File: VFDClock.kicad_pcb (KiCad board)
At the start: 2 copper layers, 76.2 x 53.3 mm, 21 parts, among them J1 Barrel_Jack_MountingPin, P1 Power, P2 Analog, P3 Digital, P4 Digital, Q1 VFD_LD8035E, Q2 VFD_LD8035E, Q3 VFD_LD8035E, Q4 VFD_LD8035E, Q5 VFD_LD8035E, Q6 VFD_LD8035E, U1 IC_HT16K33

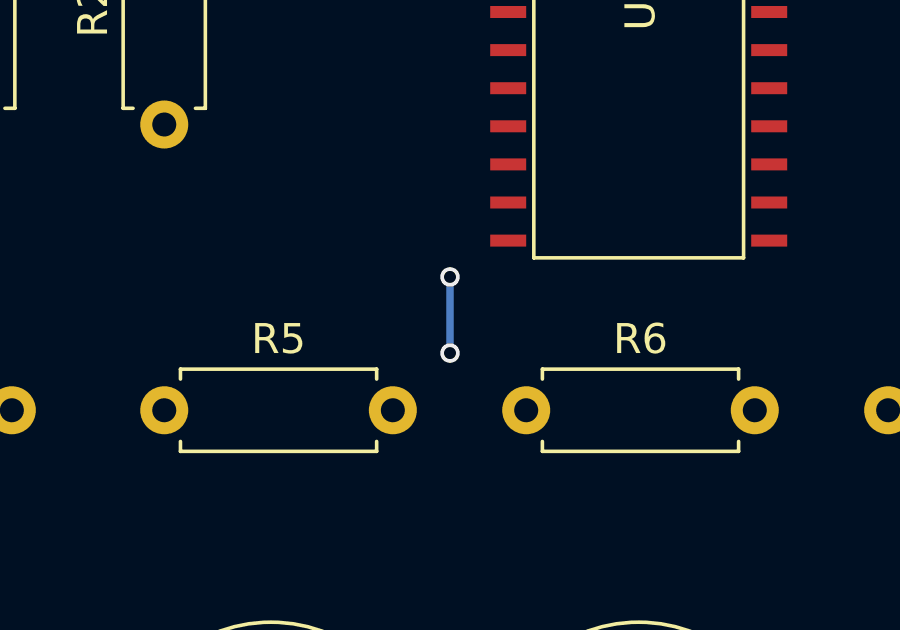
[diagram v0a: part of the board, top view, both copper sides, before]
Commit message: 余分なビアを削除
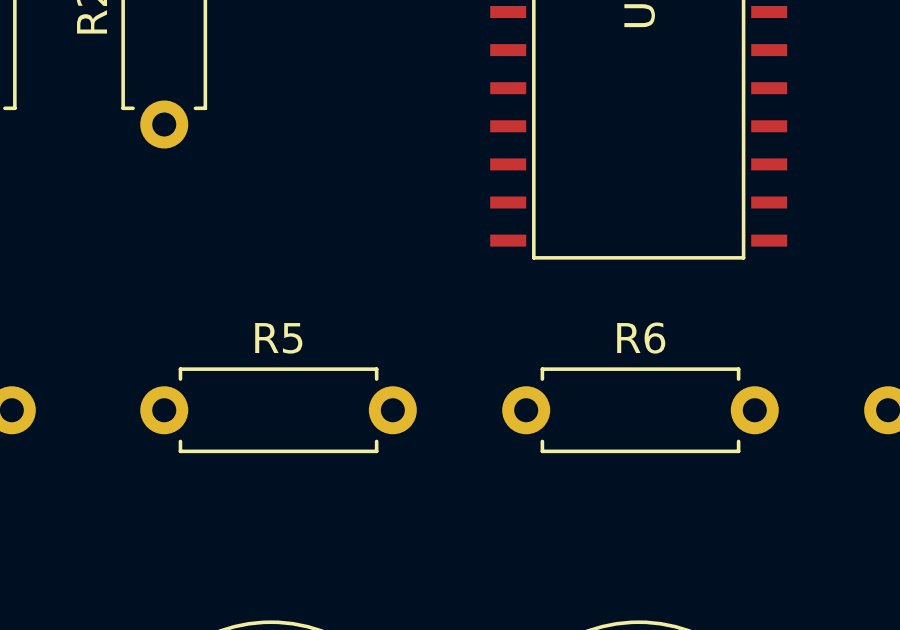
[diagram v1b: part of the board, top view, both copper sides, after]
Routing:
- net GND: track 2.54 -> 0.00 mm, vias 2 -> 0
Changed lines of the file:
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@@
     (thickness 1.6)
     (drawings 11)
-    (tracks 3)
+    (tracks 0)
     (zones 0)
     (modules 21)
@@
   (gr_line (start 175.514 73.025) (end 110.998 73.025) (angle 90) (layer Edge.Cuts) (width 0.15))
   (gr_line (start 104.648 82.55) (end 120.523 82.55) (angle 90) (layer Dwgs.User) (width 0.15))
-  (via (at 149.098 98.425) (size 0.65) (drill 0.4) (layers F.Cu B.Cu) (net 2))
-  (via (at 149.098 100.965) (size 0.65) (drill 0.4) (layers F.Cu B.Cu) (net 2))
-  (segment (start 149.098 98.425) (end 149.098 100.965) (width 0.25) (layer B.Cu) (net 2))
 )

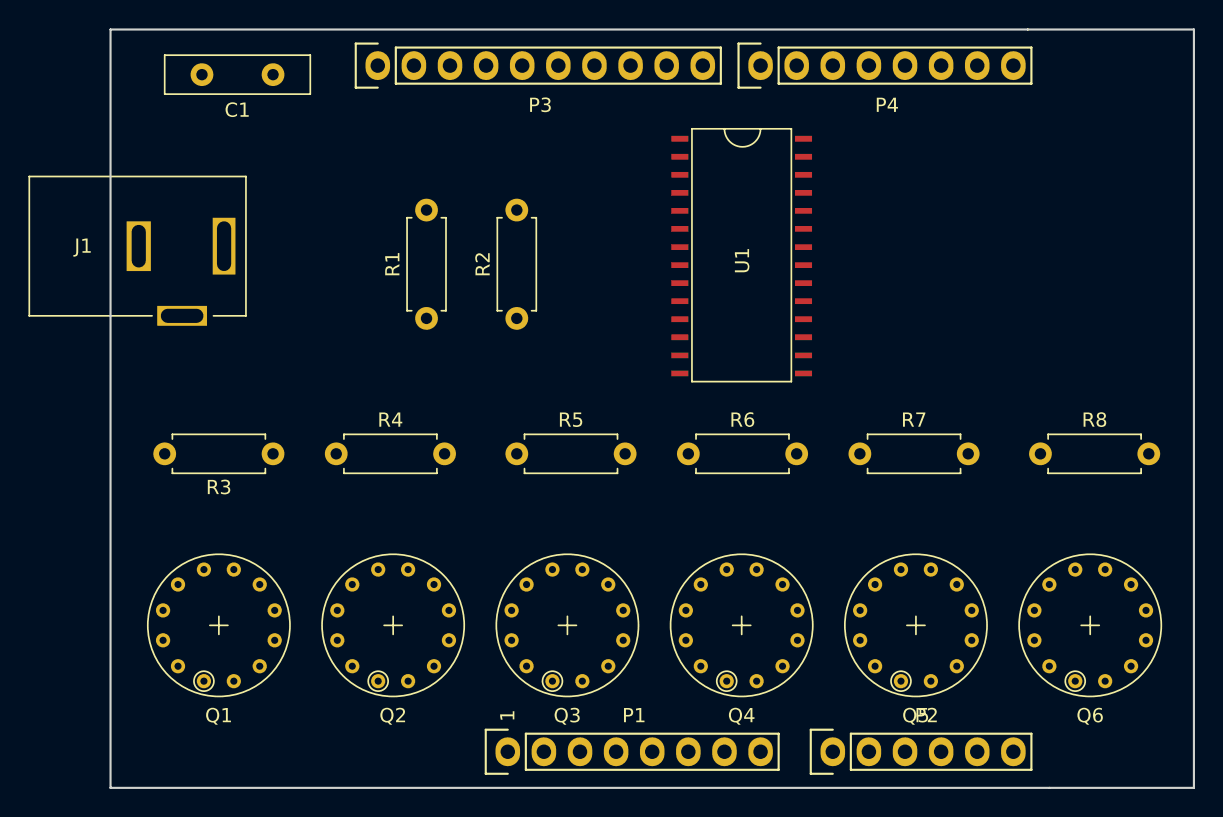
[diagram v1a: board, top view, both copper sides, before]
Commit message: RTCを追加
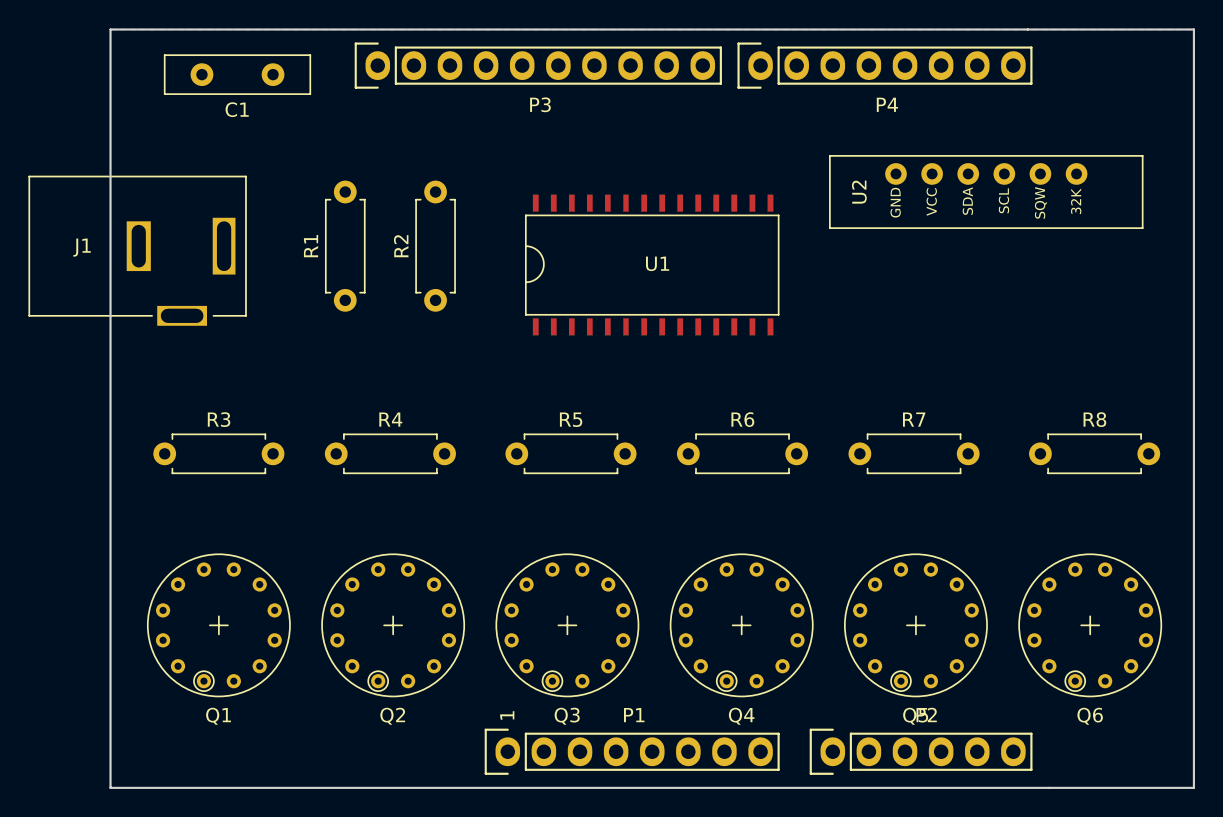
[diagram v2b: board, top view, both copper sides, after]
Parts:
- added U2: RTC_DS3231, #MyFootPrints:RTC_DS3231_Vertical, F.Cu at (172.6, 87.0)
- moved U1 17.6 mm to (140.2, 93.3), turned to 90 degrees
- moved R3 7.62 mm to (114.8, 102.9), turned to 0 degrees
- moved R1 5.85 mm to (127.5, 92.1)
- moved R2 5.85 mm to (133.9, 92.1)
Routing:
- added copper zone on B.Cu, net GND
- added copper zone on F.Cu, net GND
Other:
- net class GND added: clearance 0.2, trace_width 0.6, via_dia 0.65, via_drill 0.4

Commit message: 自動配線
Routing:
- net /a: track 0.00 -> 121.7 mm
- net /dp: track 0.00 -> 120.7 mm
- net /e: track 0.00 -> 118.6 mm
- net /d: track 0.00 -> 115.2 mm, vias 0 -> 1
- net +5V: track 0.00 -> 105.8 mm
- net /c: track 0.00 -> 104.7 mm, vias 0 -> 1
- net +12V: track 0.00 -> 102.9 mm
- net /g: track 0.00 -> 102.6 mm, vias 0 -> 1
- net /b: track 0.00 -> 102.1 mm, vias 0 -> 1
- net /f: track 0.00 -> 96.1 mm, vias 0 -> 1
- net Net-(Q5-Pad3): track 0.00 -> 69.1 mm
- net /A5(SCL): track 0.00 -> 61.6 mm
- net Net-(Q6-Pad3): track 0.00 -> 50.7 mm
- net /A4(SDA): track 0.00 -> 49.7 mm
- net Net-(Q1-Pad3): track 0.00 -> 35.3 mm, vias 0 -> 1
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
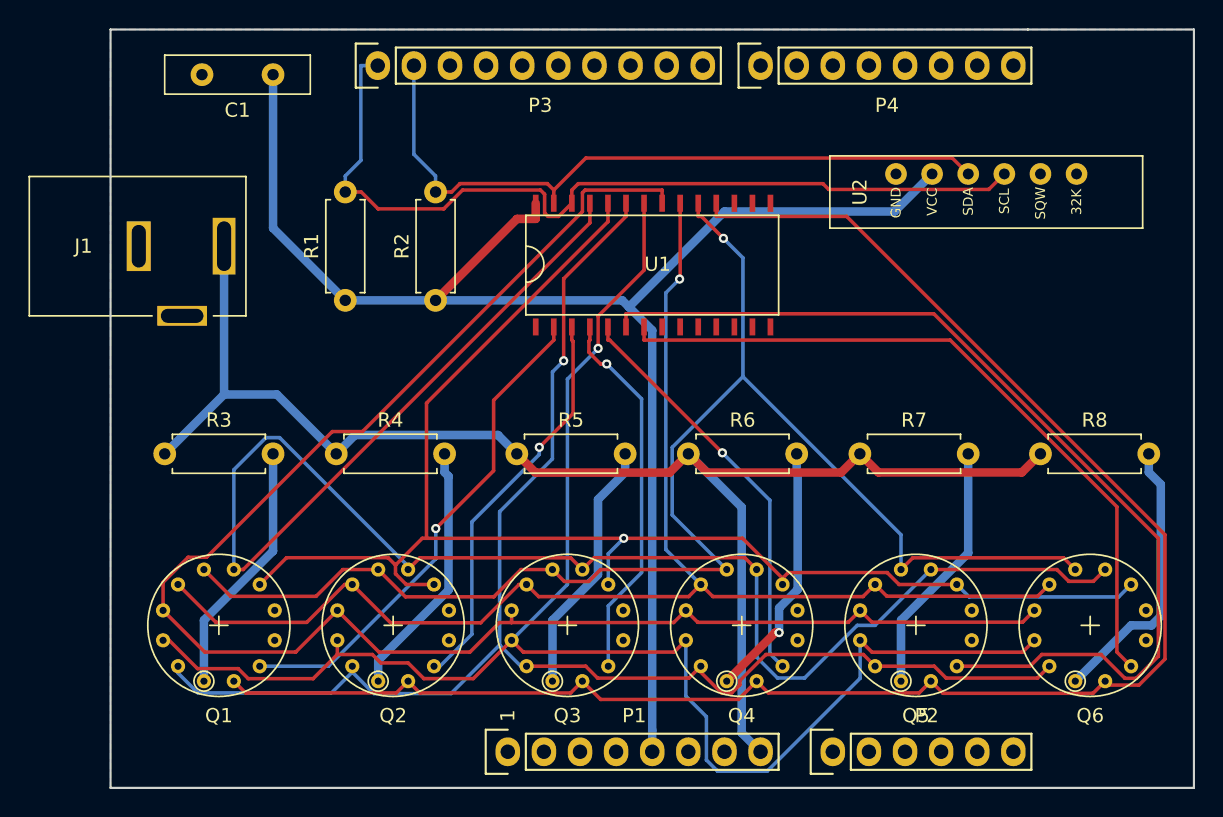
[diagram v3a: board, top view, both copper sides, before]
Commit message: 配線を修正
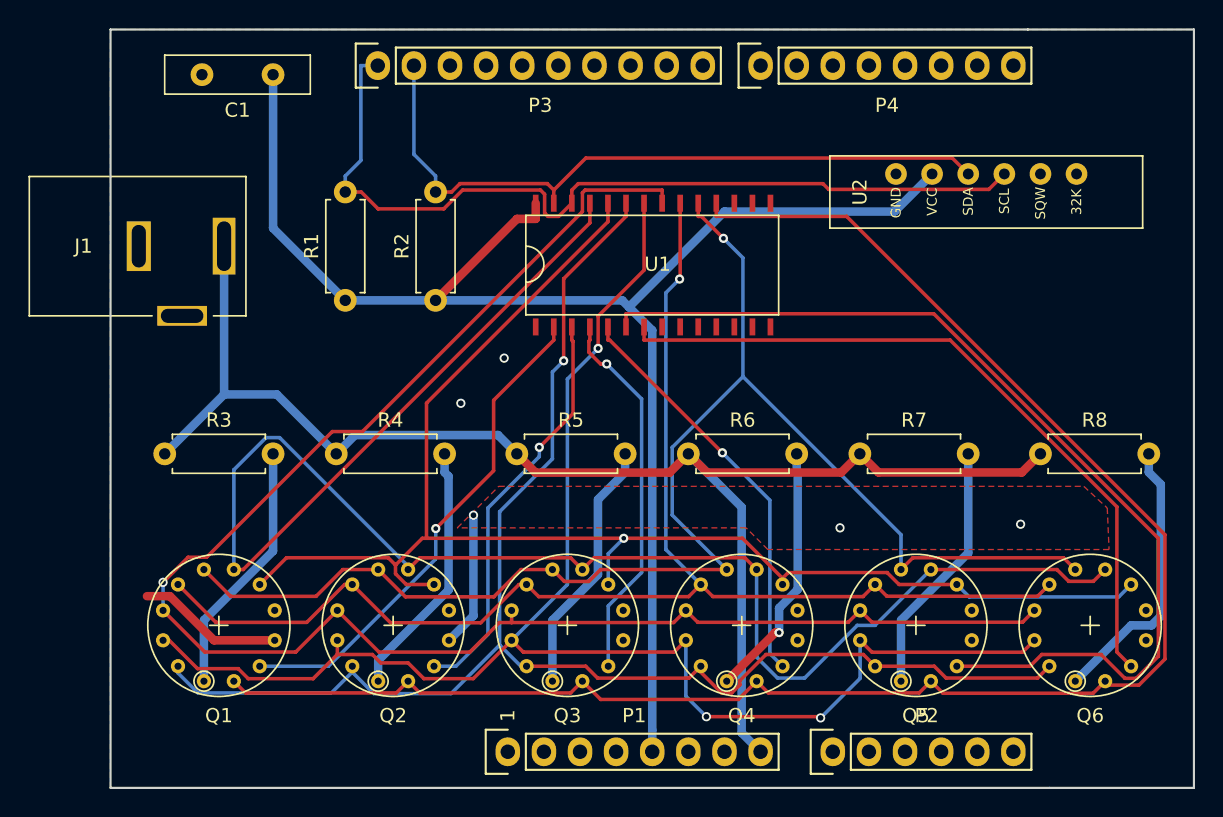
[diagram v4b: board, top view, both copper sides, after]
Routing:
- net GND: track 0.00 -> 19.8 mm, vias 0 -> 5
- net /d: track 115.2 -> 110.3 mm, vias 1 -> 3
- net Net-(Q2-Pad3): track 28.2 -> 29.3 mm
- net /e: vias 0 -> 1

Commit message: GND修正
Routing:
- net GND: track 19.8 -> 47.5 mm, vias 5 -> 4
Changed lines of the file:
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@@
     (thickness 1.6)
     (drawings 11)
-    (tracks 375)
+    (tracks 382)
     (zones 0)
     (modules 22)
@@
   (segment (start 122.428 86.995) (end 127.508 92.075) (width 0.6) (layer B.Cu) (net 1))
   (segment (start 140.903 85.245) (end 140.903 86.3453) (width 0.6) (layer F.Cu) (net 1))
-  (via (at 138.684 96.139) (size 0.65) (drill 0.4) (layers F.Cu B.Cu) (net 2))
-  (via (at 135.636 99.314) (size 0.65) (drill 0.4) (layers F.Cu B.Cu) (net 2))
-  (via (at 162.306 108.077) (size 0.65) (drill 0.4) (layers F.Cu B.Cu) (net 2))
-  (via (at 175.006 107.823) (size 0.65) (drill 0.4) (layers F.Cu B.Cu) (net 2))
   (segment (start 115.172478 112.883158) (end 113.557842 112.883158) (width 0.6) (layer F.Cu) (net 2))
   (segment (start 122.543523 115.986841) (end 118.276161 115.986841) (width 0.6) (layer F.Cu) (net 2))
   (segment (start 118.276161 115.986841) (end 115.172478 112.883158) (width 0.6) (layer F.Cu) (net 2))
-  (segment (start 134.800523 115.986841) (end 136.525 114.262364) (width 0.6) (layer B.Cu) (net 2))
-  (segment (start 136.525 114.262364) (end 136.525 107.188) (width 0.6) (layer B.Cu) (net 2))
-  (segment (start 136.525 107.188) (end 136.525 107.188) (width 0.6) (layer B.Cu) (net 2))
-  (via (at 136.525 107.188) (size 0.65) (drill 0.4) (layers F.Cu B.Cu) (net 2))
+  (segment (start 136.525 102.743) (end 136.525 102.743) (width 0.6) (layer B.Cu) (net 2))
+  (via (at 136.525 102.743) (size 0.65) (drill 0.4) (layers F.Cu B.Cu) (net 2))
+  (segment (start 136.525 98.323) (end 140.903 93.945) (width 0.6) (layer F.Cu) (net 2))
+  (segment (start 136.525 102.743) (end 136.525 98.323) (width 0.6) (layer F.Cu) (net 2))
+  (segment (start 136.525 114.262364) (end 134.800523 115.986841) (width 0.6) (layer B.Cu) (net 2))
+  (segment (start 136.525 102.743) (end 136.525 114.262364) (width 0.6) (layer B.Cu) (net 2))
+  (segment (start 136.525 98.323) (end 136.525 98.323) (width 0.6) (layer F.Cu) (net 2))
+  (via (at 136.525 98.323) (size 0.65) (drill 0.4) (layers F.Cu B.Cu) (net 2))
+  (segment (start 159.314523 115.986841) (end 161.925 113.376364) (width 0.6) (layer B.Cu) (net 2))
+  (segment (start 161.925 113.376364) (end 161.925 109.474) (width 0.6) (layer B.Cu) (net 2))
+  (segment (start 161.925 109.474) (end 161.925 109.474) (width 0.6) (layer B.Cu) (net 2))
+  (via (at 161.925 109.474) (size 0.65) (drill 0.4) (layers F.Cu B.Cu) (net 2))
+  (segment (start 161.925 109.474) (end 165.481 105.918) (width 0.6) (layer F.Cu) (net 2))
+  (segment (start 165.481 105.918) (end 165.481 105.918) (width 0.6) (layer F.Cu) (net 2))
+  (via (at 165.481 105.918) (size 0.65) (drill 0.4) (layers F.Cu B.Cu) (net 2))
   (segment (start 133.858 84.455) (end 133.858 83.3297) (width 0.25) (layer B.Cu) (net 3))
   (segment (start 132.334 75.565) (end 132.334 81.8057) (width 0.25) (layer B.Cu) (net 3))
@@
   (segment (start 184.8673 114.2873) (end 184.8673 105.0146) (width 0.6) (layer B.Cu) (net 25))
   (segment (start 184.8673 105.0146) (end 184.023 104.1703) (width 0.6) (layer B.Cu) (net 25))
-  (zone (net 2) (net_name GND) (layer B.Cu) (hatch edge 0.508)
-    (connect_pads (clearance 0.508))
-    (min_thickness 0.254)
-    (fill yes (arc_segments 32) (thermal_gap 0.508) (thermal_bridge_width 0.508))
-    (polygon
-      (pts
-        (xy 187.198 126.365) (xy 110.998 126.365) (xy 110.998 73.025) (xy 187.198 73.025)
-      )
-    )
-  )
   (zone (net 2) (net_name GND) (layer F.Cu) (hatch edge 0.508)
     (connect_pads (clearance 0.508))
@@
       (pts
         (xy 187.198 126.365) (xy 110.998 126.365) (xy 110.998 73.025) (xy 187.198 73.025)
-      )
-    )
-  )
-  (zone (net 0) (net_name "") (layer F.Cu) (hatch edge 0.508)
-    (connect_pads (clearance 0.508))
-    (min_thickness 0.254)
-    (keepout (tracks allowed) (vias allowed) (copperpour not_allowed))
-    (fill (arc_segments 32) (thermal_gap 0.508) (thermal_bridge_width 0.508))
-    (polygon
-      (pts
-        (xy 142.113 92.71) (xy 140.843 92.71) (xy 142.113 91.44)
-      )
-    )
-  )
-  (zone (net 0) (net_name "") (layer F.Cu) (hatch edge 0.508)
-    (connect_pads (clearance 0.508))
-    (min_thickness 0.254)
-    (keepout (tracks allowed) (vias allowed) (copperpour not_allowed))
-    (fill (arc_segments 32) (thermal_gap 0.508) (thermal_bridge_width 0.508))
-    (polygon
-      (pts
-        (xy 142.494 93.218) (xy 140.462 93.218) (xy 140.462 92.837) (xy 142.113 91.186) (xy 142.367 91.186)
-      )
-    )
-  )
-  (zone (net 2) (net_name GND) (layer F.Cu) (hatch edge 0.508)
-    (connect_pads (clearance 0.508))
-    (min_thickness 0.254)
-    (fill yes (arc_segments 32) (thermal_gap 0.508) (thermal_bridge_width 0.508))
-    (polygon
-      (pts
-        (xy 181.102 106.68) (xy 181.229 109.601) (xy 157.226 109.601) (xy 155.702 108.077) (xy 135.382 108.077)
-        (xy 138.303 105.156) (xy 179.451 105.156)
       )
     )
@@
       )
     )
+  )
+  (zone (net 2) (net_name GND) (layer B.Cu) (hatch edge 0.508)
+    (connect_pads (clearance 0.508))
+    (min_thickness 0.254)
+    (fill yes (arc_segments 32) (thermal_gap 0.508) (thermal_bridge_width 0.508))
+    (polygon
+      (pts
+        (xy 187.198 126.365) (xy 110.998 126.365) (xy 110.998 73.025) (xy 187.198 73.025)
+      )
+    )
+  )
+  (zone (net 0) (net_name "") (layer B.Cu) (hatch edge 0.508)
+    (connect_pads (clearance 0.508))
+    (min_thickness 0.254)
+    (keepout (tracks allowed) (vias allowed) (copperpour not_allowed))
+    (fill (arc_segments 32) (thermal_gap 0.508) (thermal_bridge_width 0.508))
+    (polygon
+      (pts
+        (xy 138.43 103.124) (xy 139.446 104.14) (xy 137.16 106.68) (xy 137.033 115.316) (xy 135.89 116.586)
+        (xy 134.874 114.808) (xy 135.382 104.013) (xy 135.636 102.235) (xy 138.049 102.108)
+      )
+    )
+  )
+  (zone (net 0) (net_name "") (layer B.Cu) (hatch edge 0.508)
+    (connect_pads (clearance 0.508))
+    (min_thickness 0.254)
+    (keepout (tracks allowed) (vias allowed) (copperpour not_allowed))
+    (fill (arc_segments 32) (thermal_gap 0.508) (thermal_bridge_width 0.508))
+    (polygon
+      (pts
+        (xy 165.608 108.458) (xy 159.893 117.729) (xy 157.861 116.84) (xy 159.766 112.649) (xy 159.766 103.886)
+        (xy 160.274 103.251)
+      )
+    )
+  )
+  (zone (net 0) (net_name "") (layer F.Cu) (hatch edge 0.508)
+    (connect_pads (clearance 0.508))
+    (min_thickness 0.254)
+    (keepout (tracks allowed) (vias allowed) (copperpour not_allowed))
+    (fill (arc_segments 32) (thermal_gap 0.508) (thermal_bridge_width 0.508))
+    (polygon
+      (pts
+        (xy 141.224 95.25) (xy 137.668 98.679) (xy 137.541 103.886) (xy 133.731 107.442) (xy 133.731 99.568)
+        (xy 141.224 92.202)
+      )
+    )
+  )
+  (zone (net 0) (net_name "") (layer F.Cu) (hatch edge 0.508)
+    (connect_pads (clearance 0.508))
+    (min_thickness 0.254)
+    (keepout (tracks allowed) (vias allowed) (copperpour not_allowed))
+    (fill (arc_segments 32) (thermal_gap 0.508) (thermal_bridge_width 0.508))
+    (polygon
+      (pts
+        (xy 157.353 120.142) (xy 162.306 120.142) (xy 161.544 120.904) (xy 155.448 121.031) (xy 155.321 120.65)
+        (xy 156.21 119.761) (xy 156.464 119.634)
+      )
+    )
+  )
+  (zone (net 0) (net_name "") (layer F.Cu) (hatch edge 0.508)
+    (connect_pads (clearance 0.508))
+    (min_thickness 0.254)
+    (keepout (tracks allowed) (vias allowed) (copperpour not_allowed))
+    (fill (arc_segments 32) (thermal_gap 0.508) (thermal_bridge_width 0.508))
+    (polygon
+      (pts
+        (xy 181.483 106.68) (xy 181.356 109.982) (xy 180.086 111.125) (xy 178.308 109.982) (xy 167.386 109.855)
+        (xy 166.116 110.744) (xy 158.115 110.998) (xy 155.575 108.458) (xy 134.239 108.331) (xy 138.684 103.759)
+        (xy 140.462 104.648) (xy 174.371 104.775) (xy 177.673 103.251)
+      )
+    )
